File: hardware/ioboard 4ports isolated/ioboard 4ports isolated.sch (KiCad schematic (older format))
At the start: 30 parts, among them J1 Conn_02x06_Odd_Even, J10 XLR3, J2 Conn_01x03, J3 XLR3, J4 Conn_01x03, J5 XLR3, J7 XLR3, U1 M24C02-WMN, U2 ADM2483xRW, U3 CRE1S0505DC, U4 ADM2483xRW

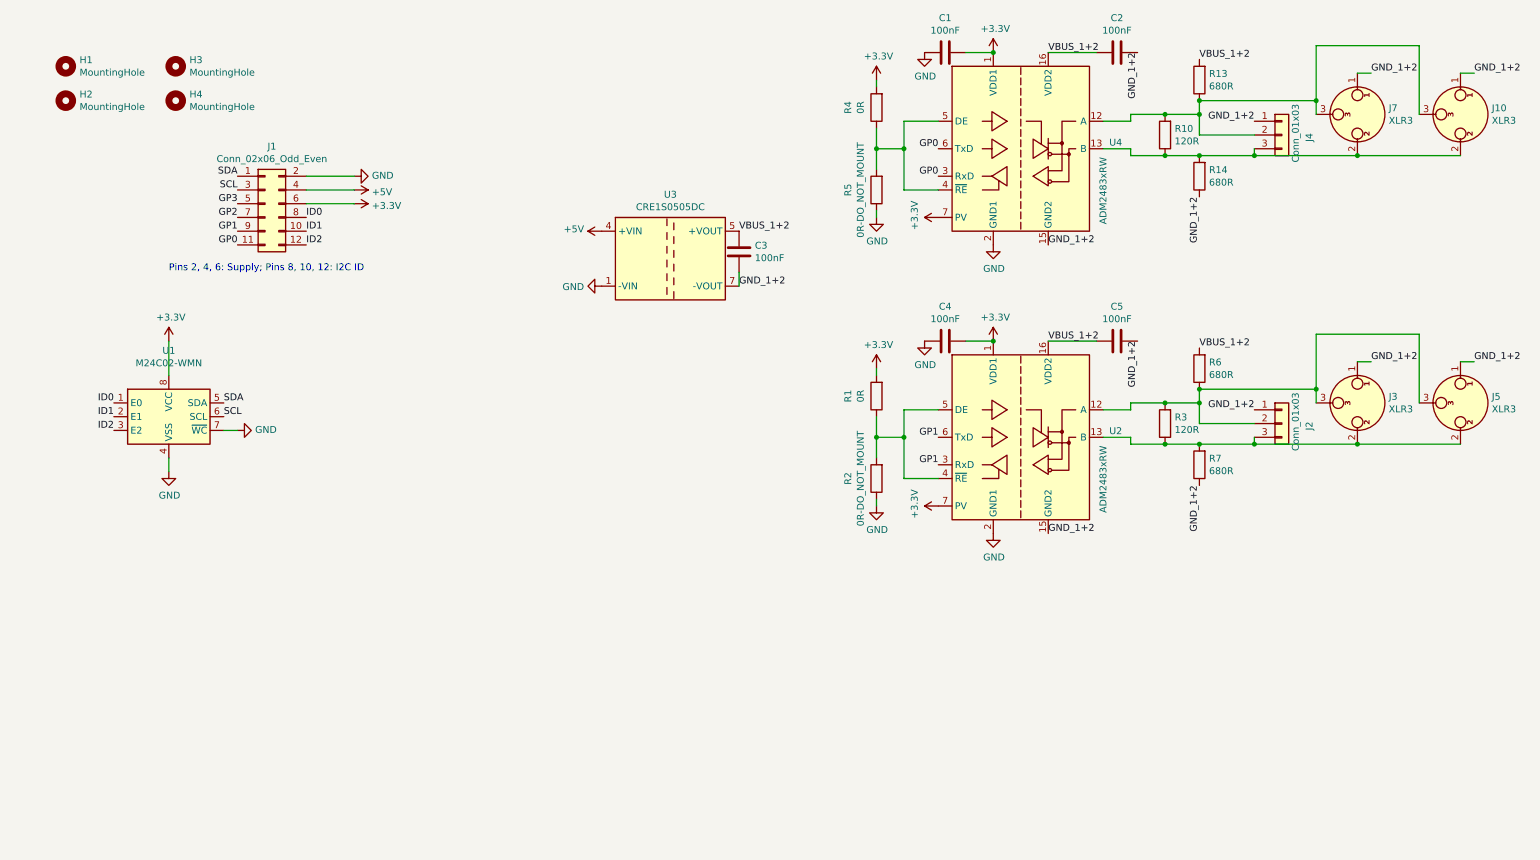
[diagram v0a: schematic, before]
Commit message: Finish ioboard 4ports isolated
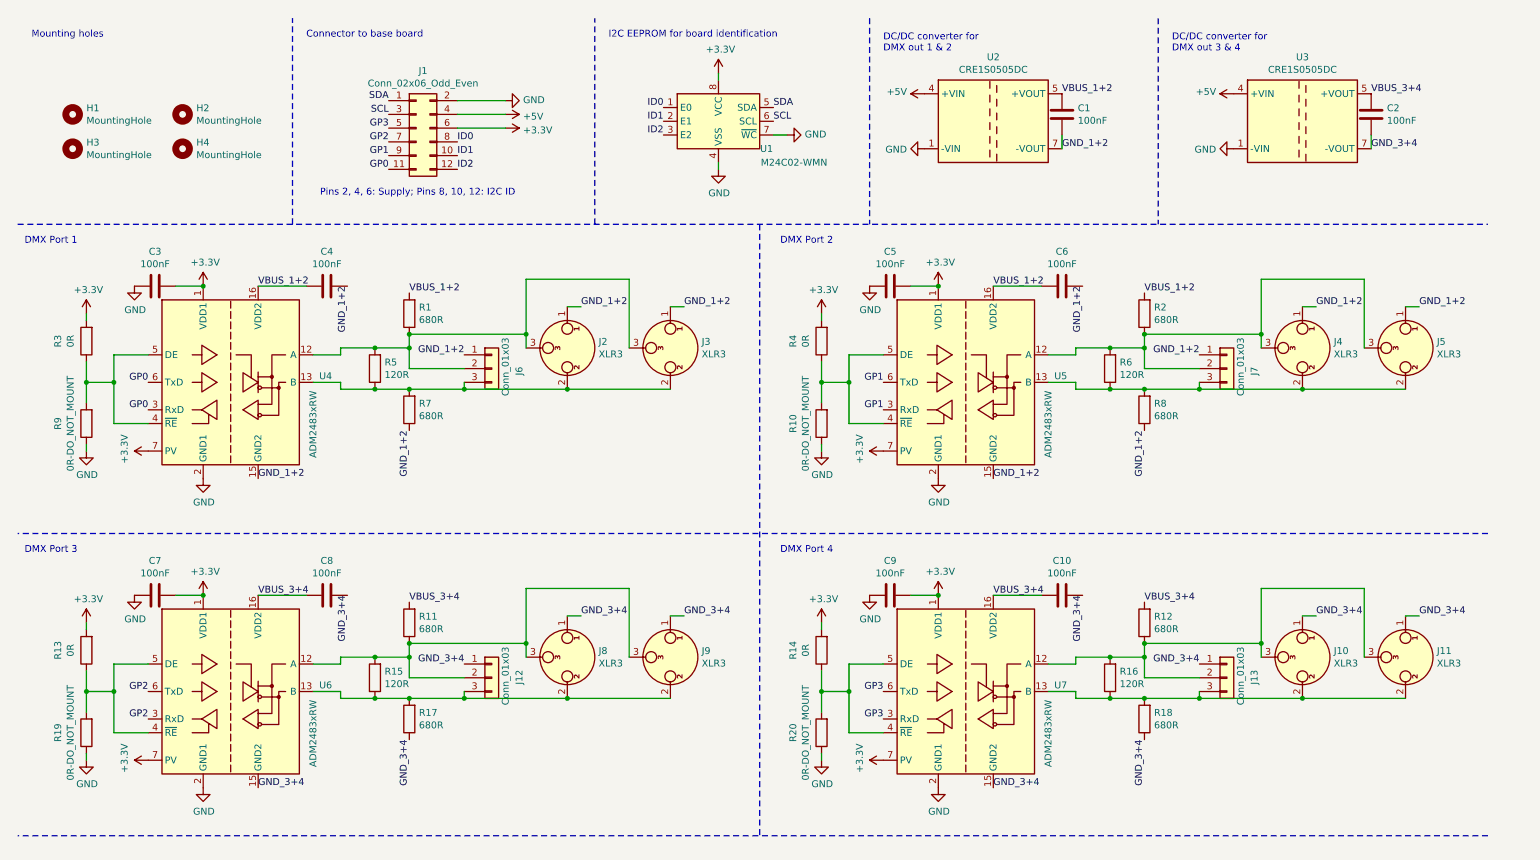
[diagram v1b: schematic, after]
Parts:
- added C10, C2, C7, C8, C9: 100nF, Capacitor_SMD:C_0603_1608Metric, symbol Device:C
- added J10, J8: XLR3, Connector_Audio:Jack_XLR_Neutrik_NC3FAAH_Horizontal, symbol Connector:XLR3
- added J11, J9: XLR3, NC3FD-H:Jack_XLR_Neutrik_NC3FD-H_Horizontal, symbol Connector:XLR3
- added J12, J13: Conn_01x03, Connector_PinHeader_2.54mm:PinHeader_1x03_P2.54mm_Vertical, symbol Connector_Generic:Conn_01x03
- added R11, R12, R17, R18: 680R, Resistor_SMD:R_0603_1608Metric_Pad0.98x0.95mm_HandSolder, symbol Device:R
- added R13, R14: 0R, Resistor_SMD:R_0603_1608Metric_Pad0.98x0.95mm_HandSolder, symbol Device:R
- added R15, R16: 120R, Resistor_SMD:R_0603_1608Metric_Pad0.98x0.95mm_HandSolder, symbol Device:R
- added R19, R20: 0R-DO_NOT_MOUNT, Resistor_SMD:R_0603_1608Metric_Pad0.98x0.95mm_HandSolder, symbol Device:R
- added U3: CRE1S0505DC, Converter_DCDC:Converter_DCDC_muRata_CRE1xxxxxxDC_THT, symbol Regulator_Switching:CRE1S0505DC
- added U6, U7: ADM2483xRW, Package_SO:SOIC-16W_7.5x10.3mm_P1.27mm, symbol Interface_UART:ADM2483xRW
- renumbered C3 to C1, C1 to C3, C2 to C4, C4 to C5, C5 to C6, H3 to H2, H2 to H3, J7 to J2, J10 to J3, J3 to J4, J4 to J6, J2 to J7, R13 to R1, R2 to R10, R6 to R2, R4 to R3, R1 to R4, R10 to R5, R3 to R6, R14 to R7, R7 to R8, R5 to R9, U3 to U2, U2 to U5
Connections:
- net +3V3: now also C7.1, C9.1, R13.2, R14.2, U6.1 (VDD1), U6.7 (PV), U7.1 (VDD1), U7.7 (PV)
- net +5V: now also U3.4 (+VIN)
- net GND: now also C7.2, C9.2, R19.1, R20.1, U3.1 (-VIN), U6.2 (GND1), U6.8 (GND1), U7.2 (GND1), U7.8 (GND1)
- net GP2: now also U6.3 (RxD), U6.6 (TxD)
- net GP3: now also U7.3 (RxD), U7.6 (TxD)
- new net: R13.1, R19.2, U6.4 (~RE), U6.5 (DE)
- new net: J12.3 (Pin_3), J8.2, J9.2, R15.1, R17.2, U6.13 (B)
- new net: J12.2 (Pin_2), J8.3, J9.3, R11.1, R15.2, U6.12 (A)
- new net: R14.1, R20.2, U7.4 (~RE), U7.5 (DE)
- new net: J10.2, J11.2, J13.3 (Pin_3), R16.1, R18.2, U7.13 (B)
- new net: J10.3, J11.3, J13.2 (Pin_2), R12.1, R16.2, U7.12 (A)
- new net GND_3+4: C10.1, C2.1, C8.1, J10.1, J11.1, J12.1 (Pin_1), J13.1 (Pin_1), J8.1, J9.1, R17.1, R18.1, U3.7 (-VOUT), U6.15 (GND2), U6.9 (GND2), U7.15 (GND2), U7.9 (GND2)
- new net VBUS_3+4: C10.2, C2.2, C8.2, R11.2, R12.2, U3.5 (+VOUT), U6.16 (VDD2), U7.16 (VDD2)
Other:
- note added: "Connector to base board"
- note added: "DC/DC converter for\nDMX out 1 & 2"
- note added: "DC/DC converter for\nDMX out 3 & 4"
- note added: "DMX Port 1"
- note added: "DMX Port 2"
- note added: "DMX Port 3"
- note added: "DMX Port 4"
- note added: "I2C EEPROM for board identification"
- note added: "Mounting holes"
- moved on the sheet: C1, C3, C4, C5, C6, H1, H2, H3, H4, J1, J2, J3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

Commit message: Hardware: Several fixes and improvements in schematics and PCBs (more capacitors, alternative footprint for DC/DC converter, more GND stitching, better trace placement, ...)
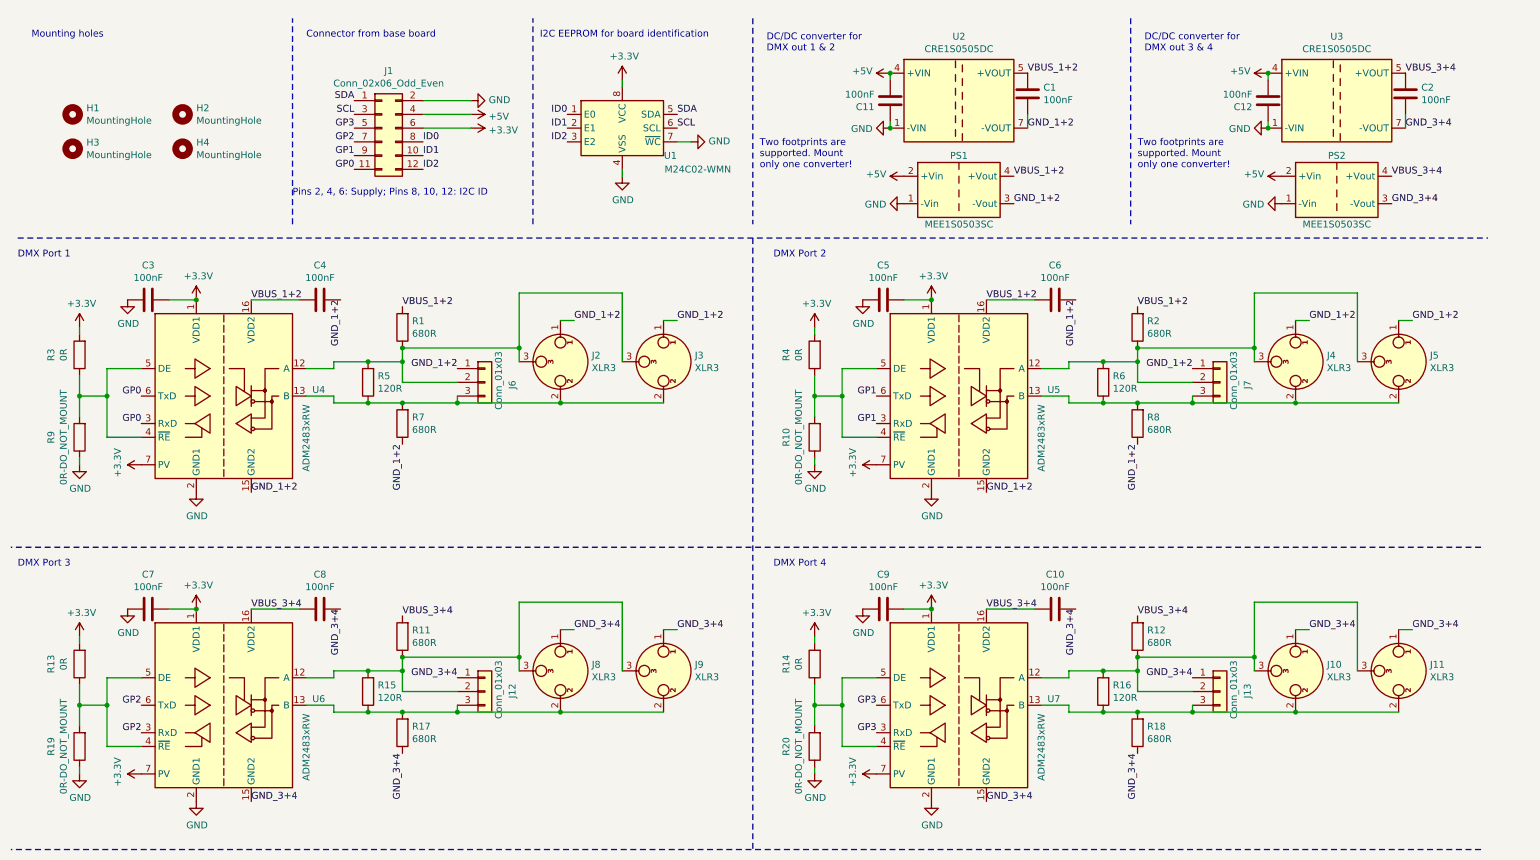
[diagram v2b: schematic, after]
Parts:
- added C11, C12: 100nF, Capacitor_SMD:C_0603_1608Metric, symbol Device:C
- added PS1, PS2: MEE1S0503SC, Converter_DCDC:Converter_DCDC_muRata_CRE1xxxxxx3C_THT, symbol Converter_DCDC:MEE1S0503SC
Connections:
- net +5V: now also C11.1, C12.1, PS1.2 (+Vin), PS2.2 (+Vin)
- net GND: now also C11.2, C12.2, PS1.1 (-Vin), PS2.1 (-Vin)
- net GND_1+2: now also PS1.3 (-Vout)
- net GND_3+4: now also PS2.3 (-Vout)
- net VBUS_1+2: now also PS1.4 (+Vout)
- net VBUS_3+4: now also PS2.4 (+Vout)
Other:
- note added: "Connector from base board"
- note added: "Two footprints are\nsupported. Mount\nonly one converter!"
- note removed: "Connector to base board"
- moved on the sheet: C1, C10, C2, C3, C4, C5, C6, C7, C8, C9, J1, J10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

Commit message: Add LCSC part numbers to the schematic for production :)
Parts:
- C1, C10, C11, C12, C2, C3, C4, C5, C6, C7, C8, C9: LCSC (none) -> C14663
- R1, R11, R12, R17, R18, R2, R7, R8: LCSC (none) -> C23228
- R10, R13, R14, R19, R20, R3, R4, R9: footprint Resistor_SMD:R_0603_1608Metric_Pad0.98x0.95mm_HandSolder -> Resistor_SMD:R_0805_2012Metric_Pad1.20x1.40mm_HandSolder; LCSC (none) -> C17477
- R15, R16, R5, R6: LCSC (none) -> C22787
- U1: LCSC (none) -> C7562
- U4, U5, U6, U7: LCSC (none) -> C9637
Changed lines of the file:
@@
 F 2 "Package_SO:SOIC-8_3.9x4.9mm_P1.27mm" H 4900 1650 50  0001 C CNN
 F 3 "http://www.st.com/content/ccc/resource/technical/document/datasheet/b0/d8/50/40/5a/85/49/6f/DM00071904.pdf/files/DM00071904.pdf/jcr:content/translations/en.DM00071904.pdf" H 4950 800 50  0001 C CNN
+F 4 "C7562" H 4900 1300 50  0001 C CNN "LCSC"
 	1    4900 1300
 	1    0    0    -1
@@
 F 0 "R9" V 1157 3550 50  0000 C CNN
 F 1 "0R-DO_NOT_MOUNT" V 1066 3550 50  0000 C CNN
-F 2 "Resistor_SMD:R_0603_1608Metric_Pad0.98x0.95mm_HandSolder" V 880 3550 50  0001 C CNN
+F 2 "Resistor_SMD:R_0805_2012Metric_Pad1.20x1.40mm_HandSolder" V 880 3550 50  0001 C CNN
 F 3 "~" H 950 3550 50  0001 C CNN
+F 4 "C17477" V 950 3550 50  0001 C CNN "LCSC"
 	1    950  3550
 	-1   0    0    1
@@
 F 0 "R3" V 1157 2950 50  0000 C CNN
 F 1 "0R" V 1066 2950 50  0000 C CNN
-F 2 "Resistor_SMD:R_0603_1608Metric_Pad0.98x0.95mm_HandSolder" V 880 2950 50  0001 C CNN
+F 2 "Resistor_SMD:R_0805_2012Metric_Pad1.20x1.40mm_HandSolder" V 880 2950 50  0001 C CNN
 F 3 "~" H 950 2950 50  0001 C CNN
+F 4 "C17477" V 950 2950 50  0001 C CNN "LCSC"
 	1    950  2950
 	-1   0    0    1
@@
 F 2 "Resistor_SMD:R_0603_1608Metric_Pad0.98x0.95mm_HandSolder" V 2980 3150 50  0001 C CNN
 F 3 "~" H 3050 3150 50  0001 C CNN
+F 4 "C22787" H 3050 3150 50  0001 C CNN "LCSC"
 	1    3050 3150
 	-1   0    0    1
@@
 F 2 "Package_SO:SOIC-16W_7.5x10.3mm_P1.27mm" H 2000 2550 50  0001 C CNN
 F 3 "https://www.analog.com/media/en/technical-documentation/data-sheets/adm2483.pdf" H 1250 3300 50  0001 C CNN
+F 4 "C9637" H 2000 3250 50  0001 C CNN "LCSC"
 	1    2000 3250
 	1    0    0    -1
@@
 F 2 "Resistor_SMD:R_0603_1608Metric_Pad0.98x0.95mm_HandSolder" V 3230 2750 50  0001 C CNN
 F 3 "~" H 3300 2750 50  0001 C CNN
+F 4 "C23228" H 3300 2750 50  0001 C CNN "LCSC"
 	1    3300 2750
 	-1   0    0    1
@@
 F 2 "Resistor_SMD:R_0603_1608Metric_Pad0.98x0.95mm_HandSolder" V 3230 3450 50  0001 C CNN
 F 3 "~" H 3300 3450 50  0001 C CNN
+F 4 "C23228" H 3300 3450 50  0001 C CNN "LCSC"
 	1    3300 3450
 	-1   0    0    1
@@
 F 2 "Capacitor_SMD:C_0603_1608Metric" H 1488 2400 50  0001 C CNN
 F 3 "~" H 1450 2550 50  0001 C CNN
+F 4 "C14663" V 1450 2550 50  0001 C CNN "LCSC"
 	1    1450 2550
 	0    1    1    0
@@
 F 2 "Capacitor_SMD:C_0603_1608Metric" H 2738 2400 50  0001 C CNN
 F 3 "~" H 2700 2550 50  0001 C CNN
+F 4 "C14663" V 2700 2550 50  0001 C CNN "LCSC"
 	1    2700 2550
 	0    1    1    0
@@
 F 0 "R10" V 6507 3550 50  0000 C CNN
 F 1 "0R-DO_NOT_MOUNT" V 6416 3550 50  0000 C CNN
-F 2 "Resistor_SMD:R_0603_1608Metric_Pad0.98x0.95mm_HandSolder" V 6230 3550 50  0001 C CNN
+F 2 "Resistor_SMD:R_0805_2012Metric_Pad1.20x1.40mm_HandSolder" V 6230 3550 50  0001 C CNN
 F 3 "~" H 6300 3550 50  0001 C CNN
+F 4 "C17477" V 6300 3550 50  0001 C CNN "LCSC"
 	1    6300 3550
 	-1   0    0    1
@@
 F 0 "R4" V 6507 2950 50  0000 C CNN
 F 1 "0R" V 6416 2950 50  0000 C CNN
-F 2 "Resistor_SMD:R_0603_1608Metric_Pad0.98x0.95mm_HandSolder" V 6230 2950 50  0001 C CNN
+F 2 "Resistor_SMD:R_0805_2012Metric_Pad1.20x1.40mm_HandSolder" V 6230 2950 50  0001 C CNN
 F 3 "~" H 6300 2950 50  0001 C CNN
+F 4 "C17477" V 6300 2950 50  0001 C CNN "LCSC"
 	1    6300 2950
 	-1   0    0    1
@@
 F 2 "Resistor_SMD:R_0603_1608Metric_Pad0.98x0.95mm_HandSolder" V 8330 3150 50  0001 C CNN
 F 3 "~" H 8400 3150 50  0001 C CNN
+F 4 "C22787" H 8400 3150 50  0001 C CNN "LCSC"
 	1    8400 3150
 	-1   0    0    1
@@
 F 2 "Package_SO:SOIC-16W_7.5x10.3mm_P1.27mm" H 7350 2550 50  0001 C CNN
 F 3 "https://www.analog.com/media/en/technical-documentation/data-sheets/adm2483.pdf" H 6600 3300 50  0001 C CNN
+F 4 "C9637" H 7350 3250 50  0001 C CNN "LCSC"
 	1    7350 3250
 	1    0    0    -1
@@
 F 2 "Resistor_SMD:R_0603_1608Metric_Pad0.98x0.95mm_HandSolder" V 8580 2750 50  0001 C CNN
 F 3 "~" H 8650 2750 50  0001 C CNN
+F 4 "C23228" H 8650 2750 50  0001 C CNN "LCSC"
 	1    8650 2750
 	-1   0    0    1
@@
 F 2 "Resistor_SMD:R_0603_1608Metric_Pad0.98x0.95mm_HandSolder" V 8580 3450 50  0001 C CNN
 F 3 "~" H 8650 3450 50  0001 C CNN
+F 4 "C23228" H 8650 3450 50  0001 C CNN "LCSC"
 	1    8650 3450
 	-1   0    0    1
@@
 F 2 "Capacitor_SMD:C_0603_1608Metric" H 6838 2400 50  0001 C CNN
 F 3 "~" H 6800 2550 50  0001 C CNN
+F 4 "C14663" V 6800 2550 50  0001 C CNN "LCSC"
 	1    6800 2550
 	0    1    1    0
@@
 F 2 "Capacitor_SMD:C_0603_1608Metric" H 8088 2400 50  0001 C CNN
 F 3 "~" H 8050 2550 50  0001 C CNN
+F 4 "C14663" V 8050 2550 50  0001 C CNN "LCSC"
 	1    8050 2550
 	0    1    1    0
@@
 F 0 "R19" V 1157 5800 50  0000 C CNN
 F 1 "0R-DO_NOT_MOUNT" V 1066 5800 50  0000 C CNN
-F 2 "Resistor_SMD:R_0603_1608Metric_Pad0.98x0.95mm_HandSolder" V 880 5800 50  0001 C CNN
+F 2 "Resistor_SMD:R_0805_2012Metric_Pad1.20x1.40mm_HandSolder" V 880 5800 50  0001 C CNN
 F 3 "~" H 950 5800 50  0001 C CNN
+F 4 "C17477" V 950 5800 50  0001 C CNN "LCSC"
 	1    950  5800
 	-1   0    0    1
@@
 F 0 "R13" V 1157 5200 50  0000 C CNN
 F 1 "0R" V 1066 5200 50  0000 C CNN
-F 2 "Resistor_SMD:R_0603_1608Metric_Pad0.98x0.95mm_HandSolder" V 880 5200 50  0001 C CNN
+F 2 "Resistor_SMD:R_0805_2012Metric_Pad1.20x1.40mm_HandSolder" V 880 5200 50  0001 C CNN
 F 3 "~" H 950 5200 50  0001 C CNN
+F 4 "C17477" V 950 5200 50  0001 C CNN "LCSC"
 	1    950  5200
 	-1   0    0    1
@@
 F 2 "Resistor_SMD:R_0603_1608Metric_Pad0.98x0.95mm_HandSolder" V 2980 5400 50  0001 C CNN
 F 3 "~" H 3050 5400 50  0001 C CNN
+F 4 "C22787" H 3050 5400 50  0001 C CNN "LCSC"
 	1    3050 5400
 	-1   0    0    1
@@
 F 2 "Package_SO:SOIC-16W_7.5x10.3mm_P1.27mm" H 2000 4800 50  0001 C CNN
 F 3 "https://www.analog.com/media/en/technical-documentation/data-sheets/adm2483.pdf" H 1250 5550 50  0001 C CNN
+F 4 "C9637" H 2000 5500 50  0001 C CNN "LCSC"
 	1    2000 5500
 	1    0    0    -1
@@
 F 2 "Resistor_SMD:R_0603_1608Metric_Pad0.98x0.95mm_HandSolder" V 3230 5000 50  0001 C CNN
 F 3 "~" H 3300 5000 50  0001 C CNN
+F 4 "C23228" H 3300 5000 50  0001 C CNN "LCSC"
 	1    3300 5000
 	-1   0    0    1
@@
 F 2 "Resistor_SMD:R_0603_1608Metric_Pad0.98x0.95mm_HandSolder" V 3230 5700 50  0001 C CNN
 F 3 "~" H 3300 5700 50  0001 C CNN
+F 4 "C23228" H 3300 5700 50  0001 C CNN "LCSC"
 	1    3300 5700
 	-1   0    0    1
@@
 F 2 "Capacitor_SMD:C_0603_1608Metric" H 1488 4650 50  0001 C CNN
 F 3 "~" H 1450 4800 50  0001 C CNN
+F 4 "C14663" V 1450 4800 50  0001 C CNN "LCSC"
 	1    1450 4800
 	0    1    1    0
@@
 F 2 "Capacitor_SMD:C_0603_1608Metric" H 2738 4650 50  0001 C CNN
 F 3 "~" H 2700 4800 50  0001 C CNN
+F 4 "C14663" V 2700 4800 50  0001 C CNN "LCSC"
 	1    2700 4800
 	0    1    1    0
@@
 F 0 "R20" V 6507 5800 50  0000 C CNN
 F 1 "0R-DO_NOT_MOUNT" V 6416 5800 50  0000 C CNN
-F 2 "Resistor_SMD:R_0603_1608Metric_Pad0.98x0.95mm_HandSolder" V 6230 5800 50  0001 C CNN
+F 2 "Resistor_SMD:R_0805_2012Metric_Pad1.20x1.40mm_HandSolder" V 6230 5800 50  0001 C CNN
 F 3 "~" H 6300 5800 50  0001 C CNN
+F 4 "C17477" V 6300 5800 50  0001 C CNN "LCSC"
 	1    6300 5800
 	-1   0    0    1
@@
 F 0 "R14" V 6507 5200 50  0000 C CNN
 F 1 "0R" V 6416 5200 50  0000 C CNN
-F 2 "Resistor_SMD:R_0603_1608Metric_Pad0.98x0.95mm_HandSolder" V 6230 5200 50  0001 C CNN
+F 2 "Resistor_SMD:R_0805_2012Metric_Pad1.20x1.40mm_HandSolder" V 6230 5200 50  0001 C CNN
 F 3 "~" H 6300 5200 50  0001 C CNN
+F 4 "C17477" V 6300 5200 50  0001 C CNN "LCSC"
 	1    6300 5200
 	-1   0    0    1
@@
 F 2 "Resistor_SMD:R_0603_1608Metric_Pad0.98x0.95mm_HandSolder" V 8330 5400 50  0001 C CNN
 F 3 "~" H 8400 5400 50  0001 C CNN
+F 4 "C22787" H 8400 5400 50  0001 C CNN "LCSC"
 	1    8400 5400
 	-1   0    0    1
@@
 F 2 "Package_SO:SOIC-16W_7.5x10.3mm_P1.27mm" H 7350 4800 50  0001 C CNN
 F 3 "https://www.analog.com/media/en/technical-documentation/data-sheets/adm2483.pdf" H 6600 5550 50  0001 C CNN
+F 4 "C9637" H 7350 5500 50  0001 C CNN "LCSC"
 	1    7350 5500
 	1    0    0    -1
@@
 F 2 "Resistor_SMD:R_0603_1608Metric_Pad0.98x0.95mm_HandSolder" V 8580 5000 50  0001 C CNN
 F 3 "~" H 8650 5000 50  0001 C CNN
+F 4 "C23228" H 8650 5000 50  0001 C CNN "LCSC"
 	1    8650 5000
 	-1   0    0    1
@@
 F 2 "Resistor_SMD:R_0603_1608Metric_Pad0.98x0.95mm_HandSolder" V 8580 5700 50  0001 C CNN
 F 3 "~" H 8650 5700 50  0001 C CNN
+F 4 "C23228" H 8650 5700 50  0001 C CNN "LCSC"
 	1    8650 5700
 	-1   0    0    1
@@
 F 2 "Capacitor_SMD:C_0603_1608Metric" H 6838 4650 50  0001 C CNN
 F 3 "~" H 6800 4800 50  0001 C CNN
+F 4 "C14663" V 6800 4800 50  0001 C CNN "LCSC"
 	1    6800 4800
 	0    1    1    0
@@
 F 2 "Capacitor_SMD:C_0603_1608Metric" H 8088 4650 50  0001 C CNN
 F 3 "~" H 8050 4800 50  0001 C CNN
+F 4 "C14663" V 8050 4800 50  0001 C CNN "LCSC"
 	1    8050 4800
 	0    1    1    0
@@
 F 2 "Capacitor_SMD:C_0603_1608Metric" H 10638 900 50  0001 C CNN
 F 3 "~" H 10600 1050 50  0001 C CNN
+F 4 "C14663" H 10600 1050 50  0001 C CNN "LCSC"
 	1    10600 1050
 	-1   0    0    1
@@
 F 2 "Capacitor_SMD:C_0603_1608Metric" H 9638 950 50  0001 C CNN
 F 3 "~" H 9600 1100 50  0001 C CNN
+F 4 "C14663" H 9600 1100 50  0001 C CNN "LCSC"
 	1    9600 1100
 	1    0    0    -1
@@
 F 2 "Capacitor_SMD:C_0603_1608Metric" H 6888 950 50  0001 C CNN
 F 3 "~" H 6850 1100 50  0001 C CNN
+F 4 "C14663" H 6850 1100 50  0001 C CNN "LCSC"
 	1    6850 1100
 	1    0    0    -1
@@
 F 2 "Capacitor_SMD:C_0603_1608Metric" H 7888 900 50  0001 C CNN
 F 3 "~" H 7850 1050 50  0001 C CNN
+F 4 "C14663" H 7850 1050 50  0001 C CNN "LCSC"
 	1    7850 1050
 	-1   0    0    1
